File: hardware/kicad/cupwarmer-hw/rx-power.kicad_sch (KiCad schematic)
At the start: 38 parts, among them J1 I2C Service, U1 STWLC38JRM

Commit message: Add VAA high-frequency bypass capacitor
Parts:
- added C25: 100nF, Capacitor_SMD:C_0603_1608Metric, symbol cupwarmer:PASSIVE_2
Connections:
- net RX_VAA: now also C25.2
- net SYS_GND: now also C25.1
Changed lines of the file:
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@@
 	)
 	(junction
+		(at 157.48 142.24)
+		(diameter 0)
+		(color 0 0 0 0)
+	)
+	(junction
 		(at 109.22 95.25)
 		(diameter 0)
@@
 	)
 	(junction
+		(at 167.64 152.4)
+		(diameter 0)
+		(color 0 0 0 0)
+	)
+	(junction
 		(at 66.04 113.03)
 		(diameter 0)
@@
 	(wire
 		(pts
+			(xy 157.48 142.24) (xy 167.64 142.24)
+		)
+		(stroke
+			(width 0)
+			(type default)
+		)
+	)
+	(wire
+		(pts
 			(xy 185.42 132.08) (xy 200.66 132.08)
 		)
@@
 	(wire
 		(pts
+			(xy 167.64 152.4) (xy 200.66 152.4)
+		)
+		(stroke
+			(width 0)
+			(type default)
+		)
+	)
+	(wire
+		(pts
 			(xy 113.03 81.28) (xy 109.22 81.28)
 		)
@@
 	(wire
 		(pts
-			(xy 157.48 152.4) (xy 200.66 152.4)
+			(xy 157.48 152.4) (xy 167.64 152.4)
 		)
 		(stroke
@@
 	(wire
 		(pts
+			(xy 156.21 142.24) (xy 157.48 142.24)
+		)
+		(stroke
+			(width 0)
+			(type default)
+		)
+	)
+	(wire
+		(pts
 			(xy 232.41 87.63) (xy 236.22 87.63)
 		)
@@
 	(global_label "RX_VAA"
 		(shape passive)
-		(at 157.48 142.24 0)
+		(at 156.21 142.24 180)
 		(effects
 			(font
 				(size 1.27 1.27)
 			)
-			(justify left)
+			(justify right)
 		)
 		(property "Intersheetrefs" "${INTERSHEET_REFS}"
-			(at 157.48 142.24 0)
+			(at 156.21 142.24 0)
 			(hide yes)
 			(show_name no)
@@
 					(unit 1)
 				)
+			)
+		)
+	)
+	(symbol
+		(lib_id "cupwarmer:PASSIVE_2")
+		(at 167.64 147.32 90)
+		(unit 1)
+		(body_style 1)
+		(exclude_from_sim no)
+		(in_bom yes)
+		(on_board yes)
+		(in_pos_files yes)
+		(dnp no)
+		(property "Reference" "C25"
+			(at 171.196 147.32 0)
+			(show_name no)
+			(do_not_autoplace no)
+			(effects
+				(font
+					(size 1.27 1.27)
+				)
+			)
+		)
+		(property "Value" "100nF"
+			(at 172.974 147.32 0)
+			(show_name no)
+			(do_not_autoplace no)
+			(effects
+				(font
+					(size 1.27 1.27)
+				)
+			)
+		)
+		(property "Footprint" "Capacitor_SMD:C_0603_1608Metric"
+			(at 167.64 147.32 -180)
+			(hide yes)
+			(show_name no)
+			(do_not_autoplace no)
+			(effects
+				(font
+					(size 1.27 1.27)
+				)
+			)
+		)
+		(property "Datasheet" "~"
+			(at 167.64 147.32 -180)
+			(hide yes)
+			(show_name no)
+			(do_not_autoplace no)
+			(effects
+				(font
+					(size 1.27 1.27)
+				)
+			)
+		)
+		(property "Description" "VAA high-frequency bypass 100nF"
+			(at 167.64 147.32 -180)
+			(hide yes)
+			(show_name no)
+			(do_not_autoplace no)
+			(effects
+				(font
+					(size 1.27 1.27)
+				)
+			)
+		)
+		(property "Manufacturer" "Wuerth Elektronik"
+			(at 3.81 0 0)
+			(hide yes)
+			(show_name no)
+			(do_not_autoplace no)
+			(effects
+				(font
+					(size 1.27 1.27)
+				)
+			)
+		)
+		(property "LCSC" "C6715111"
+			(at 3.81 0 0)
+			(hide yes)
+			(show_name no)
+			(do_not_autoplace no)
+			(effects
+				(font
+					(size 1.27 1.27)
+				)
+			)
+		)
+		(property "MPN" "885012206095"
+			(at 3.81 0 0)
+			(hide yes)
+			(show_name no)
+			(do_not_autoplace no)
+			(effects
+				(font
+					(size 1.27 1.27)
+				)
+			)
+		)
+		(pin "1"
+		)
+		(pin "2"
+		)
+		(instances
+			(project "rx-power"
+				(path "/11111111-aaaa-bbbb-cccc-111111111111"
+					(reference "C25")
+					(unit 1)
+				)
+			)
+			(project "cupwarmer-hw"
+				(path "/f3c63676-f392-4700-9f58-a6787e1eb284/11111111-1111-1111-1111-111111111111"
+					(reference "C25")
+					(unit 1)
+				)

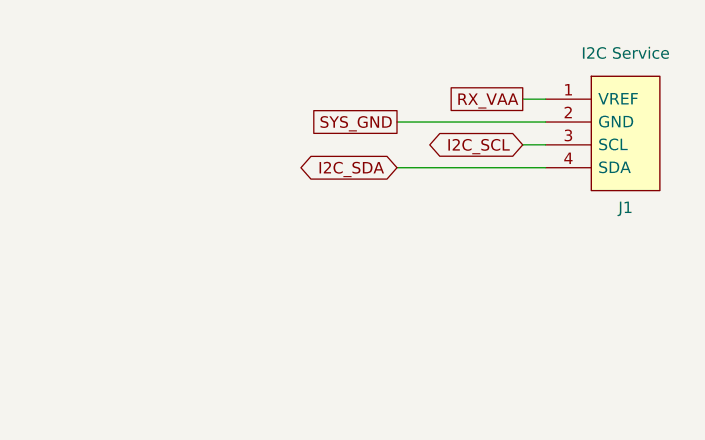
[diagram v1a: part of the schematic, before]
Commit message: Swap service I2C header pins
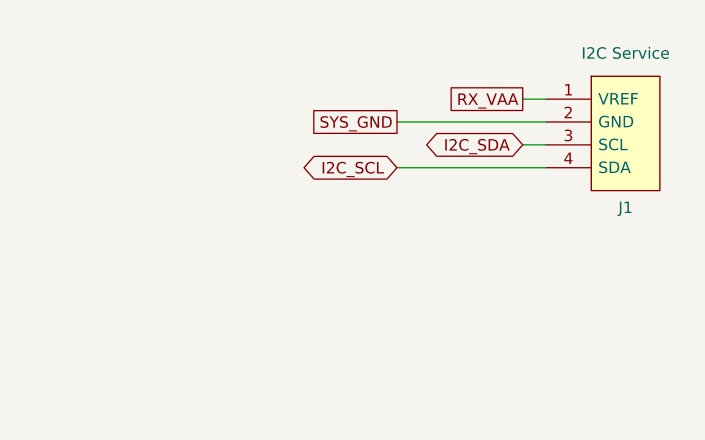
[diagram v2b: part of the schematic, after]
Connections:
- net I2C_SCL: now also J1.4 (SDA); no longer J1.3 (SCL)
- net I2C_SDA: now also J1.3 (SCL); no longer J1.4 (SDA)
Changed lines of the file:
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@@
 	(global_label "I2C_SCL"
+		(shape bidirectional)
+		(at 236.22 43.18 180)
+		(effects
+			(font
+				(size 1.27 1.27)
+			)
+			(justify right)
+		)
+		(property "Intersheetrefs" "${INTERSHEET_REFS}"
+			(at 236.22 43.18 0)
+			(hide yes)
+			(show_name no)
+			(do_not_autoplace no)
+			(effects
+				(font
+					(size 1.27 1.27)
+				)
+			)
+		)
+	)
+	(global_label "I2C_SDA"
 		(shape bidirectional)
 		(at 250.19 40.64 180)
@@
 			(hide yes)
 			(show_name no)
-			(do_not_autoplace no)
-			(effects
-				(font
-					(size 1.27 1.27)
-				)
-			)
-		)
-	)
-	(global_label "I2C_SDA"
-		(shape bidirectional)
-		(at 236.22 43.18 180)
-		(effects
-			(font
-				(size 1.27 1.27)
-			)
-			(justify right)
-		)
-		(property "Intersheetrefs" "${INTERSHEET_REFS}"
-			(at 236.22 43.18 0)
-			(hide yes)
-			(show_name no)

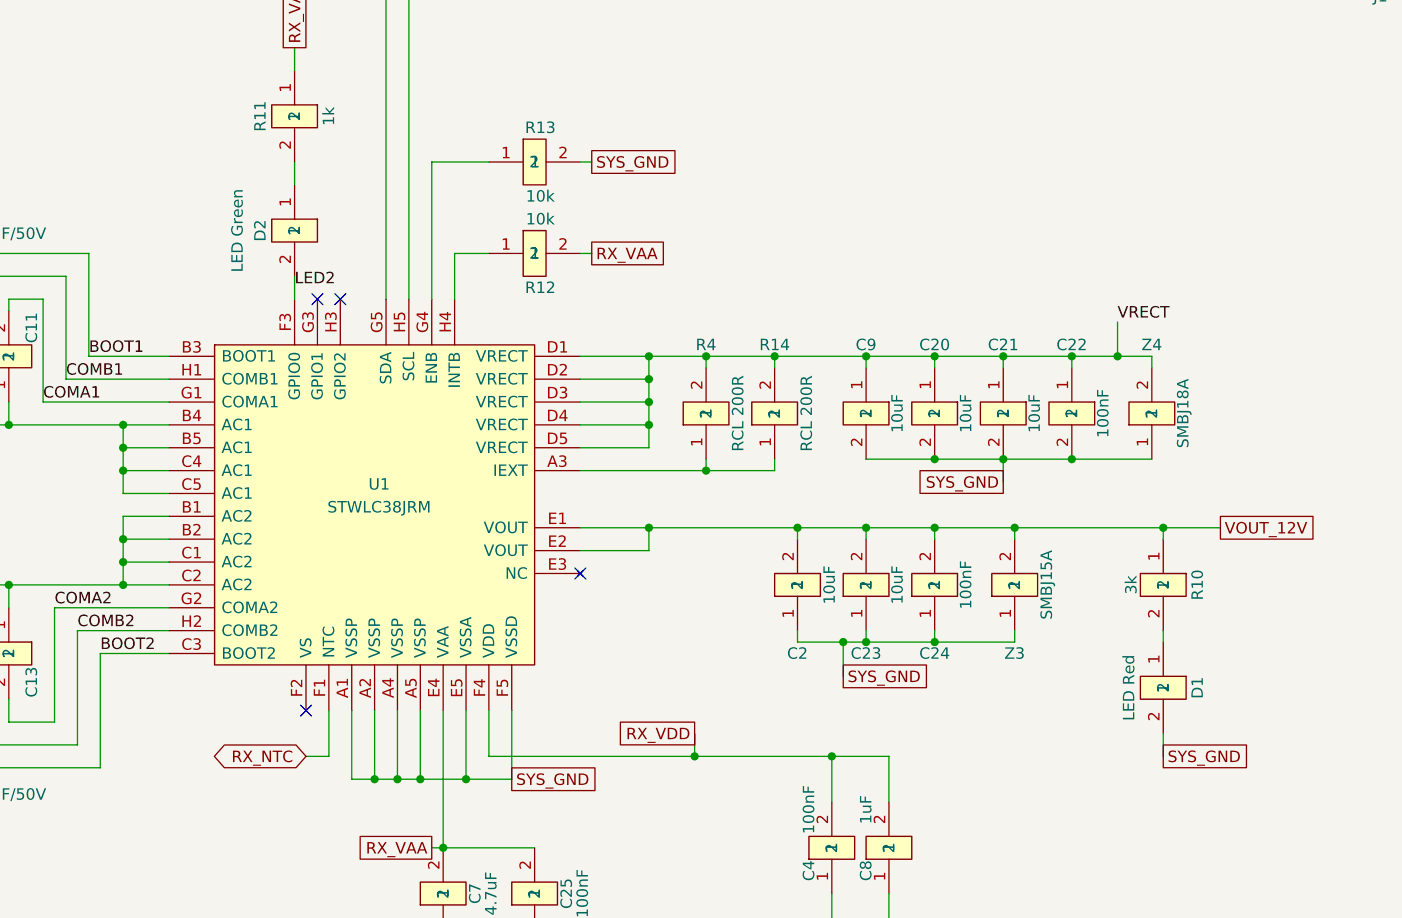
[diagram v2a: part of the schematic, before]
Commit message: Fix LED polarity and heater flyback diode
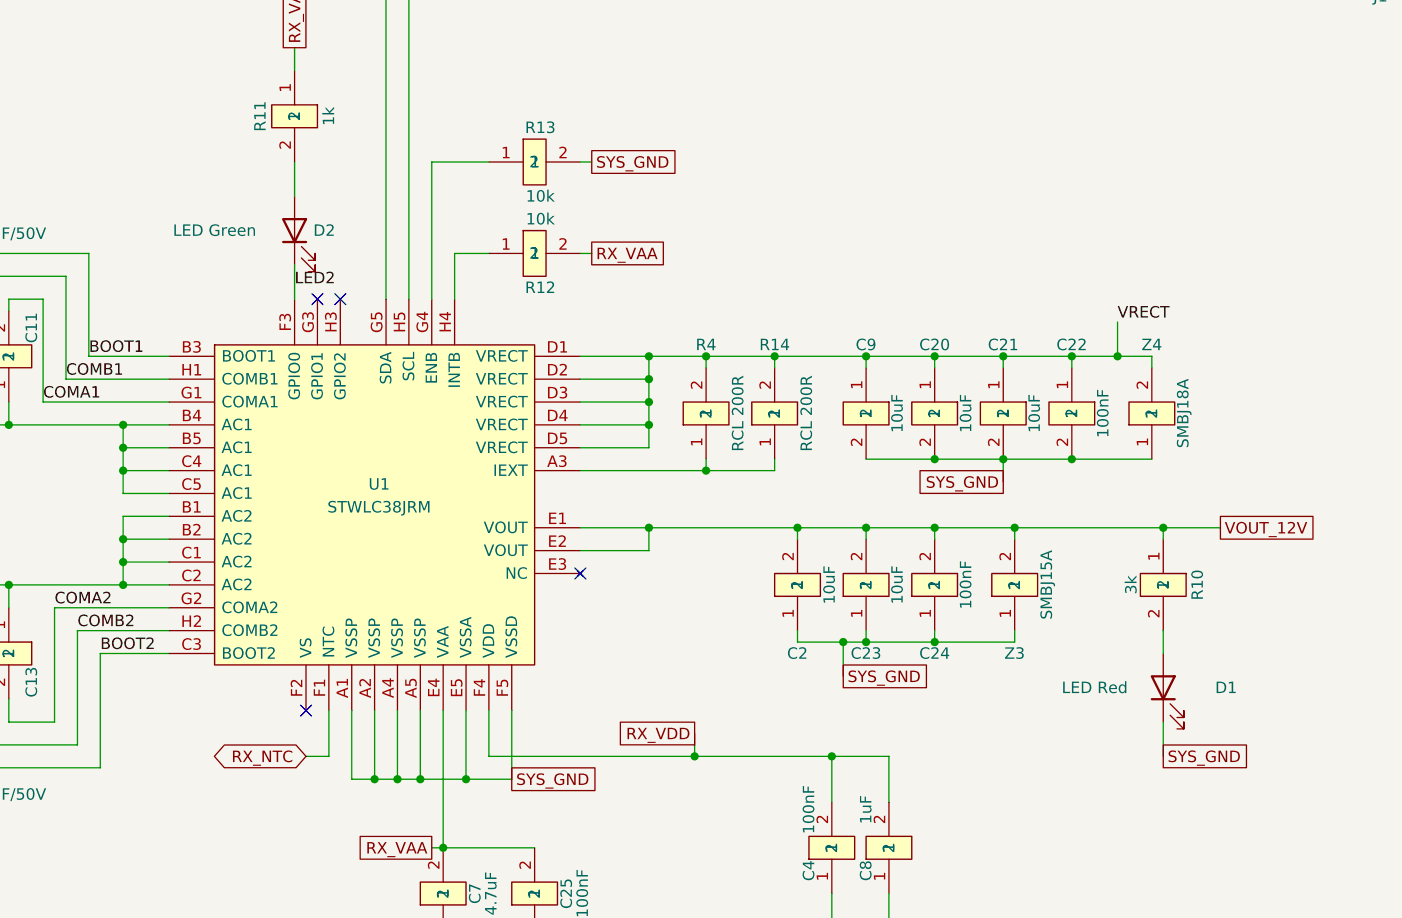
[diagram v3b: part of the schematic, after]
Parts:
- removed D1: LED Red, LED_SMD:LED_0603_1608Metric, symbol cupwarmer:PASSIVE_2
- removed D2: LED Green, LED_SMD:LED_0603_1608Metric, symbol cupwarmer:PASSIVE_2
- added D1: LED Red, LED_SMD:LED_0603_1608Metric, symbol Device:LED
- added D2: LED Green, LED_SMD:LED_0603_1608Metric, symbol Device:LED
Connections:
- net LED2: now also D2.1 (K)
- net SYS_GND: now also D1.1 (K)
- net at R11.2: now also D2.2 (A)
- net at R10.2: now also D1.2 (A)
